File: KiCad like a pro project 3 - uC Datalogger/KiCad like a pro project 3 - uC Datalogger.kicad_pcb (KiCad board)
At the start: 2 copper layers, 53.8 x 34 mm, 29 parts, among them J1 Conn_01x04_Male, J2 Conn_01x09_Male, J3 Conn_01x04_Male, J4 Conn_02x03_Odd_Even, U1 24LC1025, U2 24LC1025, U3 DS1337S+, U4 ATMEGA328P_VQFNVQFN, Y1 32.768 KHz, Y2 16 MHz

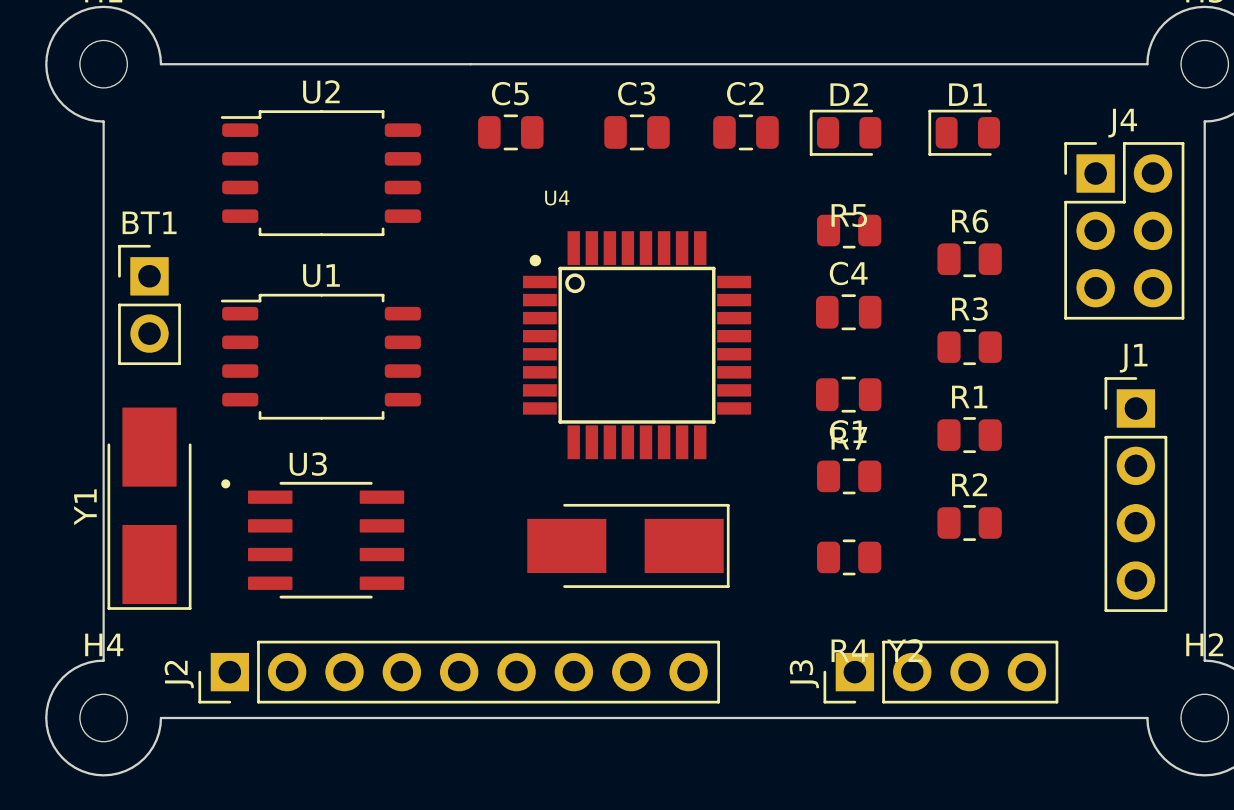
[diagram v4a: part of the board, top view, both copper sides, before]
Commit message: repositioned components and started wiring
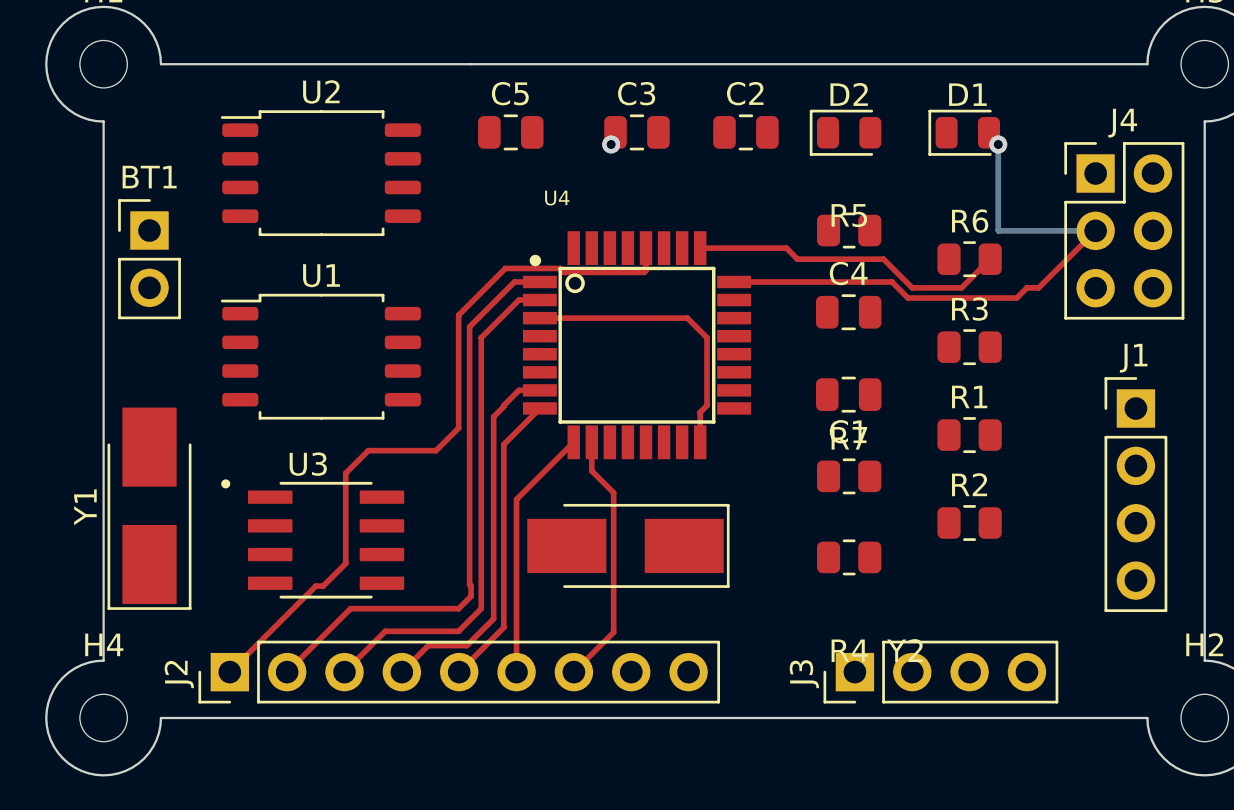
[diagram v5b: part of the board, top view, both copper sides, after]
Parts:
- moved BT1 2.03 mm to (51.3, 95.2)
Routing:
- net /D2: track 0.00 -> 32.2 mm
- net /SCL: track 0.00 -> 25.7 mm, vias 0 -> 1
- net /D3: track 0.00 -> 25.4 mm
- net /D4: track 0.00 -> 22.5 mm
- net /D5: track 0.00 -> 16.6 mm
- net /RESET: track 0.00 -> 14.1 mm
- net /D6: track 0.00 -> 13.2 mm
- net Net-(BT1-Pad1): track 0.00 -> 12.5 mm, vias 0 -> 1
- net /D8: track 0.00 -> 11.3 mm
- net /D7: track 0.00 -> 11.2 mm
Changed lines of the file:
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@@
   )
   (footprint "Connector_PinHeader_2.54mm:PinHeader_1x02_P2.54mm_Vertical" (layer "F.Cu")
-    (at 51.308 97.277)
+    (at 51.308 95.25)
     (descr "Through hole straight pin header, 1x02, 2.54mm pitch, single row")
     (tags "Through hole pin header THT 1x02 2.54mm single row")
@@
   (gr_arc (start 98.044 114.3) (mid 99.840051 118.636051) (end 95.504 116.84) (layer "Edge.Cuts") (width 0.1))
   (gr_arc (start 49.276 90.424) (mid 47.479949 86.087949) (end 51.816 87.884) (layer "Edge.Cuts") (width 0.1))
+  (segment (start 68.598 99.13) (end 75.13 99.13) (width 0.25) (layer "F.Cu") (net 1))
+  (segment (start 76 103) (end 75.698 103.302) (width 0.25) (layer "F.Cu") (net 1))
+  (segment (start 75.13 99.13) (end 76 100) (width 0.25) (layer "F.Cu") (net 1))
+  (segment (start 75.698 103.302) (end 75.698 104.63) (width 0.25) (layer "F.Cu") (net 1))
+  (segment (start 76 100) (end 76 103) (width 0.25) (layer "F.Cu") (net 1))
+  (via (at 71.755 91.44) (size 0.8) (drill 0.4) (layers "F.Cu" "B.Cu") (net 1))
+  (segment (start 84.903604 98.24) (end 89.72 98.24) (width 0.25) (layer "F.Cu") (net 8))
+  (segment (start 84.193604 97.53) (end 84.903604 98.24) (width 0.25) (layer "F.Cu") (net 8))
+  (segment (start 89.72 98.24) (end 90.17 97.79) (width 0.25) (layer "F.Cu") (net 8))
+  (segment (start 90.688 97.79) (end 93.213 95.265) (width 0.25) (layer "F.Cu") (net 8))
+  (segment (start 77.198 97.53) (end 84.193604 97.53) (width 0.25) (layer "F.Cu") (net 8))
+  (segment (start 90.17 97.79) (end 90.688 97.79) (width 0.25) (layer "F.Cu") (net 8))
+  (via (at 88.9 91.44) (size 0.8) (drill 0.4) (layers "F.Cu" "B.Cu") (net 8))
+  (segment (start 88.9 95.25) (end 88.915 95.265) (width 0.25) (layer "B.Cu") (net 8))
+  (segment (start 88.9 91.44) (end 88.9 95.25) (width 0.25) (layer "B.Cu") (net 8))
+  (segment (start 88.915 95.265) (end 93.213 95.265) (width 0.25) (layer "B.Cu") (net 8))
+  (segment (start 69.673 97.105) (end 69.498 96.93) (width 0.25) (layer "F.Cu") (net 11))
+  (segment (start 69.498 96.93) (end 67.07 96.93) (width 0.25) (layer "F.Cu") (net 11))
+  (segment (start 65 104) (end 64 105) (width 0.25) (layer "F.Cu") (net 11))
+  (segment (start 65 99) (end 65 104) (width 0.25) (layer "F.Cu") (net 11))
+  (segment (start 59 111) (end 58.672 111) (width 0.25) (layer "F.Cu") (net 11))
+  (segment (start 64 105) (end 61 105) (width 0.25) (layer "F.Cu") (net 11))
+  (segment (start 73.298 96.03) (end 73.298 97.03) (width 0.25) (layer "F.Cu") (net 11))
+  (segment (start 60 110) (end 59 111) (width 0.25) (layer "F.Cu") (net 11))
+  (segment (start 61 105) (end 60 106) (width 0.25) (layer "F.Cu") (net 11))
+  (segment (start 58.672 111) (end 54.864 114.808) (width 0.25) (layer "F.Cu") (net 11))
+  (segment (start 73.223 97.105) (end 69.673 97.105) (width 0.25) (layer "F.Cu") (net 11))
+  (segment (start 73.298 97.03) (end 73.223 97.105) (width 0.25) (layer "F.Cu") (net 11))
+  (segment (start 60 106) (end 60 110) (width 0.25) (layer "F.Cu") (net 11))
+  (segment (start 67.07 96.93) (end 65 99) (width 0.25) (layer "F.Cu") (net 11))
+  (segment (start 65.485 110.935) (end 65.485 99.515) (width 0.25) (layer "F.Cu") (net 12))
+  (segment (start 57.404 114.808) (end 60.212 112) (width 0.25) (layer "F.Cu") (net 12))
+  (segment (start 65 112) (end 65.55 111.45) (width 0.25) (layer "F.Cu") (net 12))
+  (segment (start 65.55 111) (end 65.485 110.935) (width 0.25) (layer "F.Cu") (net 12))
+  (segment (start 60.212 112) (end 65 112) (width 0.25) (layer "F.Cu") (net 12))
+  (segment (start 67.47 97.53) (end 68.598 97.53) (width 0.25) (layer "F.Cu") (net 12))
+  (segment (start 65.55 111.45) (end 65.55 111) (width 0.25) (layer "F.Cu") (net 12))
+  (segment (start 65.485 99.515) (end 67.47 97.53) (width 0.25) (layer "F.Cu") (net 12))
+  (segment (start 61.752 113) (end 65 113) (width 0.25) (layer "F.Cu") (net 13))
+  (segment (start 59.944 114.808) (end 61.752 113) (width 0.25) (layer "F.Cu") (net 13))
+  (segment (start 66 112) (end 66 100) (width 0.25) (layer "F.Cu") (net 13))
+  (segment (start 67.67 98.33) (end 68.598 98.33) (width 0.25) (layer "F.Cu") (net 13))
+  (segment (start 66 100) (end 67.67 98.33) (width 0.25) (layer "F.Cu") (net 13))
+  (segment (start 65 113) (end 66 112) (width 0.25) (layer "F.Cu") (net 13))
+  (segment (start 62.484 114.808) (end 63.659 113.633) (width 0.25) (layer "F.Cu") (net 14))
+  (segment (start 67 103.053) (end 67 103) (width 0.25) (layer "F.Cu") (net 14))
+  (segment (start 65.367 113.633) (end 66.55 112.45) (width 0.25) (layer "F.Cu") (net 14))
+  (segment (start 66.55 103.503) (end 67 103.053) (width 0.25) (layer "F.Cu") (net 14))
+  (segment (start 66.55 112.45) (end 66.55 103.503) (width 0.25) (layer "F.Cu") (net 14))
+  (segment (start 67 103) (end 67.67 102.33) (width 0.25) (layer "F.Cu") (net 14))
+  (segment (start 67.67 102.33) (end 68.598 102.33) (width 0.25) (layer "F.Cu") (net 14))
+  (segment (start 63.659 113.633) (end 65.367 113.633) (width 0.25) (layer "F.Cu") (net 14))
+  (segment (start 65.024 114.808) (end 67 112.832) (width 0.25) (layer "F.Cu") (net 15))
+  (segment (start 67 112.832) (end 67 104.728) (width 0.25) (layer "F.Cu") (net 15))
+  (segment (start 67 104.728) (end 68.598 103.13) (width 0.25) (layer "F.Cu") (net 15))
+  (segment (start 67.564 107.164) (end 70.098 104.63) (width 0.25) (layer "F.Cu") (net 16))
+  (segment (start 67.564 114.808) (end 67.564 107.164) (width 0.25) (layer "F.Cu") (net 16))
+  (segment (start 71.865 113.047) (end 71.865 106.865) (width 0.25) (layer "F.Cu") (net 17))
+  (segment (start 70.104 114.808) (end 71.865 113.047) (width 0.25) (layer "F.Cu") (net 17))
+  (segment (start 71.865 106.865) (end 70.898 105.898) (width 0.25) (layer "F.Cu") (net 17))
+  (segment (start 70.898 105.898) (end 70.898 104.63) (width 0.25) (layer "F.Cu") (net 17))
+  (segment (start 75.698 96.03) (end 79.52 96.03) (width 0.25) (layer "F.Cu") (net 22))
+  (segment (start 87.2725 97.79) (end 88.5425 96.52) (width 0.25) (layer "F.Cu") (net 22))
+  (segment (start 85.09 97.79) (end 87.2725 97.79) (width 0.25) (layer "F.Cu") (net 22))
+  (segment (start 79.52 96.03) (end 80.01 96.52) (width 0.25) (layer "F.Cu") (net 22))
+  (segment (start 83.82 96.52) (end 85.09 97.79) (width 0.25) (layer "F.Cu") (net 22))
+  (segment (start 80.01 96.52) (end 83.82 96.52) (width 0.25) (layer "F.Cu") (net 22))
 )

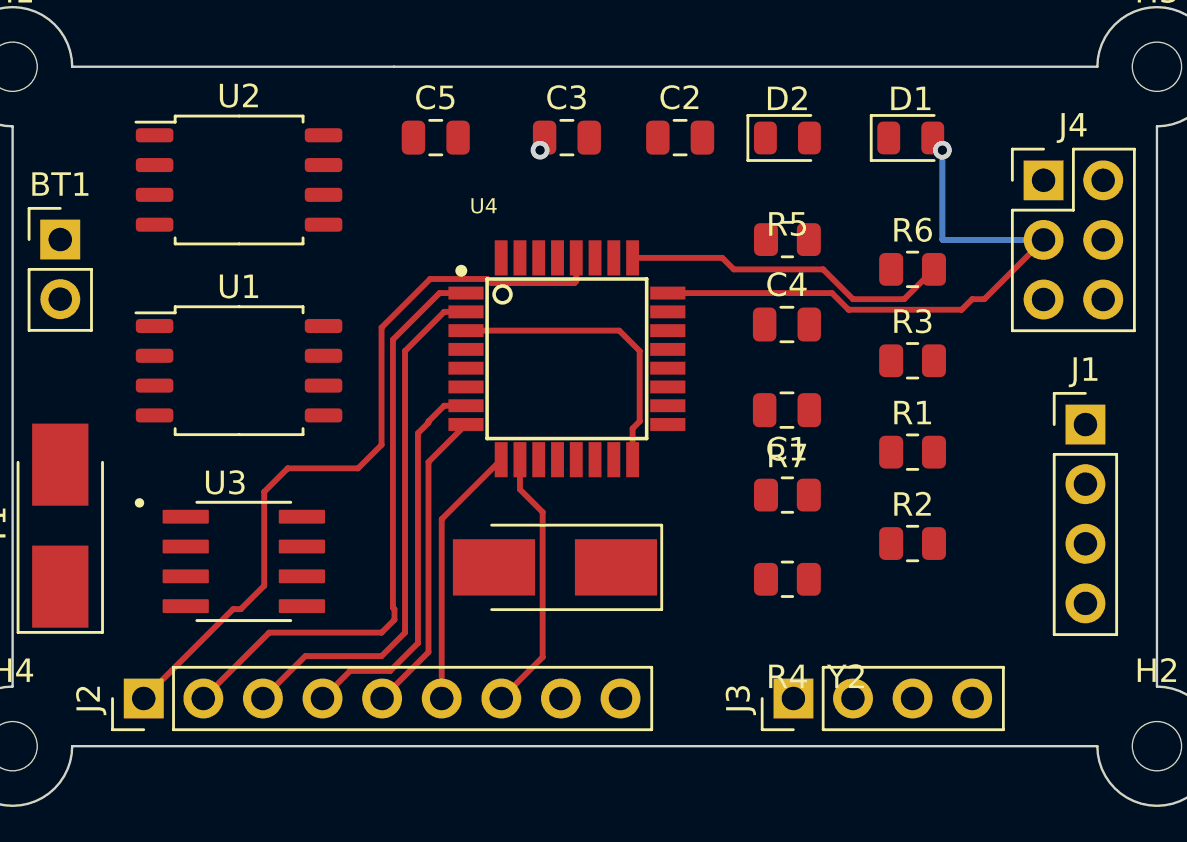
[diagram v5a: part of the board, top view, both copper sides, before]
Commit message: removed wiring
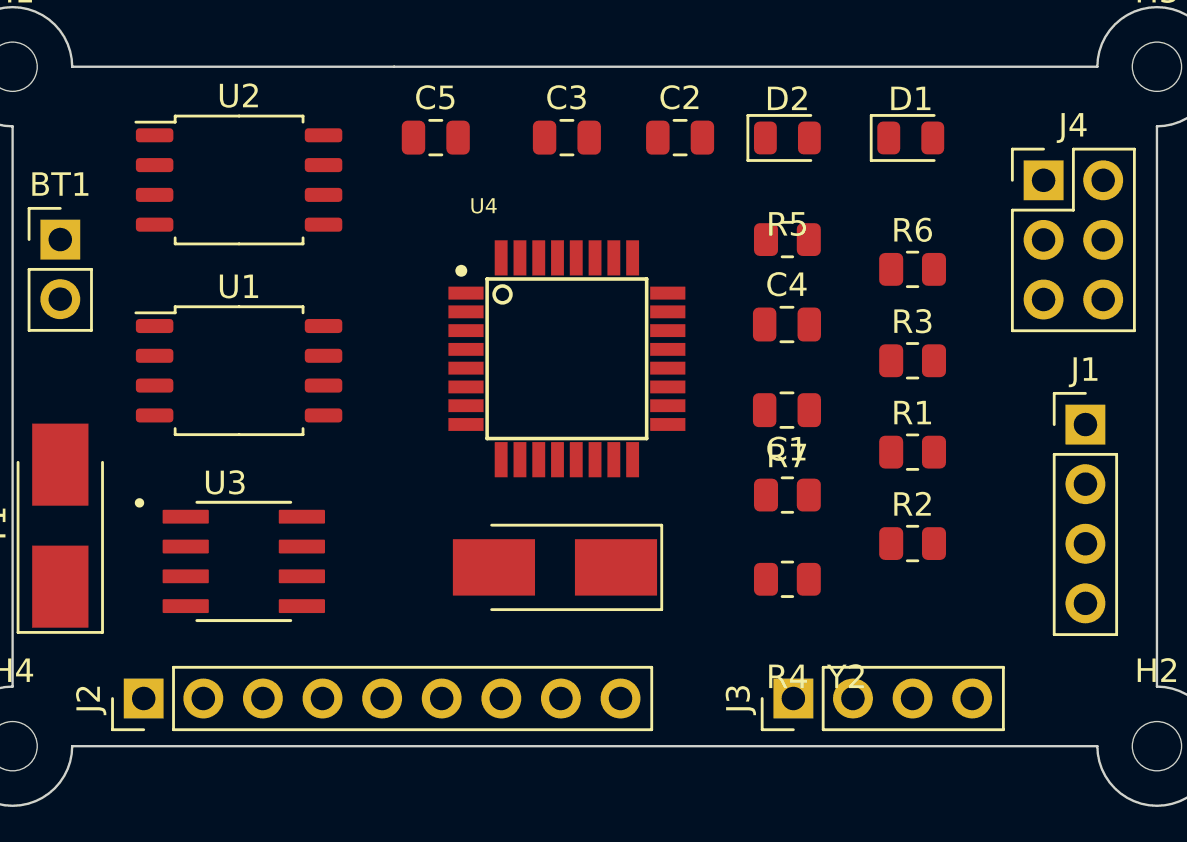
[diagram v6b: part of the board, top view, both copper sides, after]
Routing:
- net /D2: track 32.2 -> 0.00 mm
- net /SCL: track 25.7 -> 0.00 mm, vias 1 -> 0
- net /D3: track 25.4 -> 0.00 mm
- net /D4: track 22.5 -> 0.00 mm
- net /D5: track 16.6 -> 0.00 mm
- net /RESET: track 14.1 -> 0.00 mm
- net /D6: track 13.2 -> 0.00 mm
- net Net-(BT1-Pad1): track 12.5 -> 0.00 mm, vias 1 -> 0
- net /D8: track 11.3 -> 0.00 mm
- net /D7: track 11.2 -> 0.00 mm
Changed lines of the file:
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@@
   (gr_arc (start 98.044 114.3) (mid 99.840051 118.636051) (end 95.504 116.84) (layer "Edge.Cuts") (width 0.1))
   (gr_arc (start 49.276 90.424) (mid 47.479949 86.087949) (end 51.816 87.884) (layer "Edge.Cuts") (width 0.1))
-  (segment (start 68.598 99.13) (end 75.13 99.13) (width 0.25) (layer "F.Cu") (net 1))
-  (segment (start 76 103) (end 75.698 103.302) (width 0.25) (layer "F.Cu") (net 1))
-  (segment (start 75.13 99.13) (end 76 100) (width 0.25) (layer "F.Cu") (net 1))
-  (segment (start 75.698 103.302) (end 75.698 104.63) (width 0.25) (layer "F.Cu") (net 1))
-  (segment (start 76 100) (end 76 103) (width 0.25) (layer "F.Cu") (net 1))
-  (via (at 71.755 91.44) (size 0.8) (drill 0.4) (layers "F.Cu" "B.Cu") (net 1))
-  (segment (start 84.903604 98.24) (end 89.72 98.24) (width 0.25) (layer "F.Cu") (net 8))
-  (segment (start 84.193604 97.53) (end 84.903604 98.24) (width 0.25) (layer "F.Cu") (net 8))
-  (segment (start 89.72 98.24) (end 90.17 97.79) (width 0.25) (layer "F.Cu") (net 8))
-  (segment (start 90.688 97.79) (end 93.213 95.265) (width 0.25) (layer "F.Cu") (net 8))
-  (segment (start 77.198 97.53) (end 84.193604 97.53) (width 0.25) (layer "F.Cu") (net 8))
-  (segment (start 90.17 97.79) (end 90.688 97.79) (width 0.25) (layer "F.Cu") (net 8))
-  (via (at 88.9 91.44) (size 0.8) (drill 0.4) (layers "F.Cu" "B.Cu") (net 8))
-  (segment (start 88.9 95.25) (end 88.915 95.265) (width 0.25) (layer "B.Cu") (net 8))
-  (segment (start 88.9 91.44) (end 88.9 95.25) (width 0.25) (layer "B.Cu") (net 8))
-  (segment (start 88.915 95.265) (end 93.213 95.265) (width 0.25) (layer "B.Cu") (net 8))
-  (segment (start 69.673 97.105) (end 69.498 96.93) (width 0.25) (layer "F.Cu") (net 11))
-  (segment (start 69.498 96.93) (end 67.07 96.93) (width 0.25) (layer "F.Cu") (net 11))
-  (segment (start 65 104) (end 64 105) (width 0.25) (layer "F.Cu") (net 11))
-  (segment (start 65 99) (end 65 104) (width 0.25) (layer "F.Cu") (net 11))
-  (segment (start 59 111) (end 58.672 111) (width 0.25) (layer "F.Cu") (net 11))
-  (segment (start 64 105) (end 61 105) (width 0.25) (layer "F.Cu") (net 11))
-  (segment (start 73.298 96.03) (end 73.298 97.03) (width 0.25) (layer "F.Cu") (net 11))
-  (segment (start 60 110) (end 59 111) (width 0.25) (layer "F.Cu") (net 11))
-  (segment (start 61 105) (end 60 106) (width 0.25) (layer "F.Cu") (net 11))
-  (segment (start 58.672 111) (end 54.864 114.808) (width 0.25) (layer "F.Cu") (net 11))
-  (segment (start 73.223 97.105) (end 69.673 97.105) (width 0.25) (layer "F.Cu") (net 11))
-  (segment (start 73.298 97.03) (end 73.223 97.105) (width 0.25) (layer "F.Cu") (net 11))
-  (segment (start 60 106) (end 60 110) (width 0.25) (layer "F.Cu") (net 11))
-  (segment (start 67.07 96.93) (end 65 99) (width 0.25) (layer "F.Cu") (net 11))
-  (segment (start 65.485 110.935) (end 65.485 99.515) (width 0.25) (layer "F.Cu") (net 12))
-  (segment (start 57.404 114.808) (end 60.212 112) (width 0.25) (layer "F.Cu") (net 12))
-  (segment (start 65 112) (end 65.55 111.45) (width 0.25) (layer "F.Cu") (net 12))
-  (segment (start 65.55 111) (end 65.485 110.935) (width 0.25) (layer "F.Cu") (net 12))
-  (segment (start 60.212 112) (end 65 112) (width 0.25) (layer "F.Cu") (net 12))
-  (segment (start 67.47 97.53) (end 68.598 97.53) (width 0.25) (layer "F.Cu") (net 12))
-  (segment (start 65.55 111.45) (end 65.55 111) (width 0.25) (layer "F.Cu") (net 12))
-  (segment (start 65.485 99.515) (end 67.47 97.53) (width 0.25) (layer "F.Cu") (net 12))
-  (segment (start 61.752 113) (end 65 113) (width 0.25) (layer "F.Cu") (net 13))
-  (segment (start 59.944 114.808) (end 61.752 113) (width 0.25) (layer "F.Cu") (net 13))
-  (segment (start 66 112) (end 66 100) (width 0.25) (layer "F.Cu") (net 13))
-  (segment (start 67.67 98.33) (end 68.598 98.33) (width 0.25) (layer "F.Cu") (net 13))
-  (segment (start 66 100) (end 67.67 98.33) (width 0.25) (layer "F.Cu") (net 13))
-  (segment (start 65 113) (end 66 112) (width 0.25) (layer "F.Cu") (net 13))
-  (segment (start 62.484 114.808) (end 63.659 113.633) (width 0.25) (layer "F.Cu") (net 14))
-  (segment (start 67 103.053) (end 67 103) (width 0.25) (layer "F.Cu") (net 14))
-  (segment (start 65.367 113.633) (end 66.55 112.45) (width 0.25) (layer "F.Cu") (net 14))
-  (segment (start 66.55 103.503) (end 67 103.053) (width 0.25) (layer "F.Cu") (net 14))
-  (segment (start 66.55 112.45) (end 66.55 103.503) (width 0.25) (layer "F.Cu") (net 14))
-  (segment (start 67 103) (end 67.67 102.33) (width 0.25) (layer "F.Cu") (net 14))
-  (segment (start 67.67 102.33) (end 68.598 102.33) (width 0.25) (layer "F.Cu") (net 14))
-  (segment (start 63.659 113.633) (end 65.367 113.633) (width 0.25) (layer "F.Cu") (net 14))
-  (segment (start 65.024 114.808) (end 67 112.832) (width 0.25) (layer "F.Cu") (net 15))
-  (segment (start 67 112.832) (end 67 104.728) (width 0.25) (layer "F.Cu") (net 15))
-  (segment (start 67 104.728) (end 68.598 103.13) (width 0.25) (layer "F.Cu") (net 15))
-  (segment (start 67.564 107.164) (end 70.098 104.63) (width 0.25) (layer "F.Cu") (net 16))
-  (segment (start 67.564 114.808) (end 67.564 107.164) (width 0.25) (layer "F.Cu") (net 16))
-  (segment (start 71.865 113.047) (end 71.865 106.865) (width 0.25) (layer "F.Cu") (net 17))
-  (segment (start 70.104 114.808) (end 71.865 113.047) (width 0.25) (layer "F.Cu") (net 17))
-  (segment (start 71.865 106.865) (end 70.898 105.898) (width 0.25) (layer "F.Cu") (net 17))
-  (segment (start 70.898 105.898) (end 70.898 104.63) (width 0.25) (layer "F.Cu") (net 17))
-  (segment (start 75.698 96.03) (end 79.52 96.03) (width 0.25) (layer "F.Cu") (net 22))
-  (segment (start 87.2725 97.79) (end 88.5425 96.52) (width 0.25) (layer "F.Cu") (net 22))
-  (segment (start 85.09 97.79) (end 87.2725 97.79) (width 0.25) (layer "F.Cu") (net 22))
-  (segment (start 79.52 96.03) (end 80.01 96.52) (width 0.25) (layer "F.Cu") (net 22))
-  (segment (start 83.82 96.52) (end 85.09 97.79) (width 0.25) (layer "F.Cu") (net 22))
-  (segment (start 80.01 96.52) (end 83.82 96.52) (width 0.25) (layer "F.Cu") (net 22))
 )
